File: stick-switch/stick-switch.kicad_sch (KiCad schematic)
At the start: 4 parts, among them J1 Conn_01x04

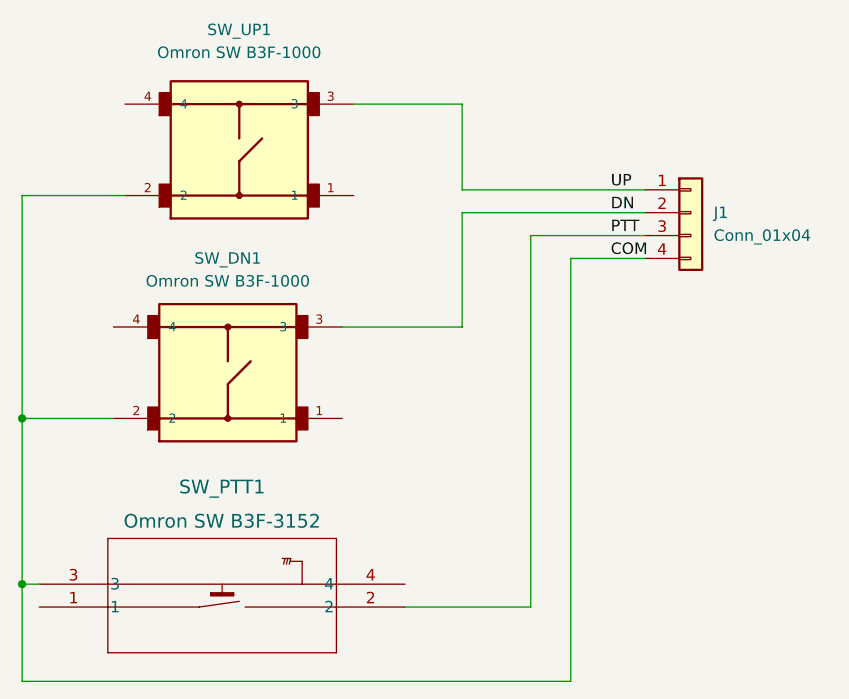
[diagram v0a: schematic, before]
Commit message: Made PTT and Trim common separate nets. Finalized layout and generated Gerbers.
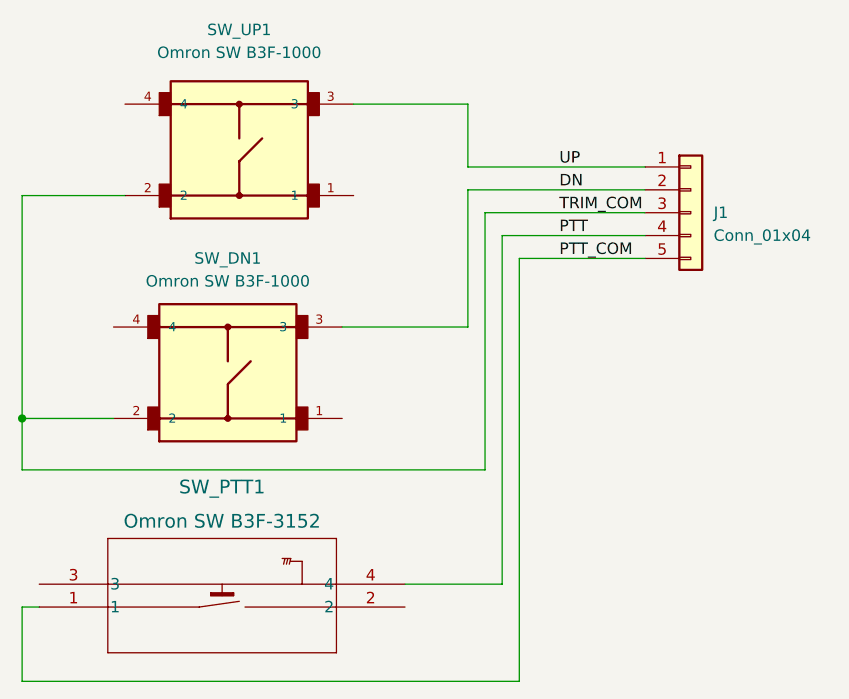
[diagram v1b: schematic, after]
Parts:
- J1: footprint Connector_PinHeader_1.27mm:PinHeader_1x04_P1.27mm_Vertical -> Connector_PinHeader_1.27mm:PinHeader_1x05_P1.27mm_Vertical; symbol Connector_Generic:Conn_01x04 -> Connector_Generic:Conn_01x05
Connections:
- net PTT: now also J1.4 (Pin_4), SW_PTT1.4; no longer J1.3 (Pin_3), SW_PTT1.2
- net PTT_COM: now reaches SW_PTT1.1
- net PTT_COM: now also J1.5 (Pin_5)
- net COM renamed TRIM_COM
- net TRIM_COM: now also J1.3 (Pin_3); no longer J1.4 (Pin_4), SW_PTT1.3
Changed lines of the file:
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@@
   (junction (at 66.675 95.25) (diameter 0) (color 0 0 0 0)
   )
-  (junction (at 66.675 113.665) (diameter 0) (color 0 0 0 0)
-  )
-  (wire (pts (xy 115.57 72.39) (xy 135.89 72.39))
+  (wire (pts (xy 116.205 69.85) (xy 135.89 69.85))
     (stroke (width 0) (type default) (color 0 0 0 0))
   )
-  (wire (pts (xy 127.635 77.47) (xy 127.635 124.46))
+  (wire (pts (xy 121.92 77.47) (xy 121.92 124.46))
     (stroke (width 0) (type default) (color 0 0 0 0))
   )
-  (wire (pts (xy 109.22 116.205) (xy 123.19 116.205))
+  (wire (pts (xy 109.22 113.665) (xy 120.015 113.665))
     (stroke (width 0) (type default) (color 0 0 0 0))
   )
@@
     (stroke (width 0) (type default) (color 0 0 0 0))
   )
-  (wire (pts (xy 115.57 60.325) (xy 115.57 69.85))
+  (wire (pts (xy 116.205 60.325) (xy 116.205 67.31))
+    (stroke (width 0) (type default) (color 0 0 0 0))
+  )
+  (wire (pts (xy 135.89 72.39) (xy 118.11 72.39))
     (stroke (width 0) (type default) (color 0 0 0 0))
   )
@@
     (stroke (width 0) (type default) (color 0 0 0 0))
   )
-  (wire (pts (xy 66.675 95.25) (xy 66.675 113.665))
+  (wire (pts (xy 103.505 60.325) (xy 116.205 60.325))
     (stroke (width 0) (type default) (color 0 0 0 0))
   )
-  (wire (pts (xy 103.505 60.325) (xy 115.57 60.325))
+  (wire (pts (xy 66.675 95.25) (xy 66.675 100.965))
     (stroke (width 0) (type default) (color 0 0 0 0))
   )
-  (wire (pts (xy 123.19 74.93) (xy 135.89 74.93))
+  (wire (pts (xy 120.015 74.93) (xy 135.89 74.93))
     (stroke (width 0) (type default) (color 0 0 0 0))
   )
-  (wire (pts (xy 115.57 69.85) (xy 135.89 69.85))
+  (wire (pts (xy 116.205 67.31) (xy 135.89 67.31))
     (stroke (width 0) (type default) (color 0 0 0 0))
   )
-  (wire (pts (xy 66.675 124.46) (xy 66.675 113.665))
+  (wire (pts (xy 66.675 124.46) (xy 66.675 116.205))
     (stroke (width 0) (type default) (color 0 0 0 0))
   )
-  (wire (pts (xy 135.89 77.47) (xy 127.635 77.47))
+  (wire (pts (xy 135.89 77.47) (xy 121.92 77.47))
     (stroke (width 0) (type default) (color 0 0 0 0))
   )
-  (wire (pts (xy 102.235 85.09) (xy 115.57 85.09))
+  (wire (pts (xy 102.235 85.09) (xy 116.205 85.09))
     (stroke (width 0) (type default) (color 0 0 0 0))
   )
-  (wire (pts (xy 66.675 113.665) (xy 68.58 113.665))
+  (wire (pts (xy 66.675 116.205) (xy 68.58 116.205))
     (stroke (width 0) (type default) (color 0 0 0 0))
   )
-  (wire (pts (xy 127.635 124.46) (xy 66.675 124.46))
+  (wire (pts (xy 118.11 100.965) (xy 66.675 100.965))
     (stroke (width 0) (type default) (color 0 0 0 0))
   )
-  (wire (pts (xy 115.57 85.09) (xy 115.57 72.39))
+  (wire (pts (xy 121.92 124.46) (xy 66.675 124.46))
     (stroke (width 0) (type default) (color 0 0 0 0))
   )
-  (wire (pts (xy 123.19 116.205) (xy 123.19 74.93))
+  (wire (pts (xy 118.11 72.39) (xy 118.11 100.965))
     (stroke (width 0) (type default) (color 0 0 0 0))
   )
-  (label "DN" (at 132.08 72.39 0)
+  (wire (pts (xy 116.205 85.09) (xy 116.205 69.85))
+    (stroke (width 0) (type default) (color 0 0 0 0))
+  )
+  (wire (pts (xy 120.015 113.665) (xy 120.015 74.93))
+    (stroke (width 0) (type default) (color 0 0 0 0))
+  )
+  (label "DN" (at 126.365 69.85 0)
     (effects (font (size 1.27 1.27)) (justify left bottom))
   )
-  (label "PTT" (at 132.08 74.93 0)
+  (label "PTT" (at 126.365 74.93 0)
     (effects (font (size 1.27 1.27)) (justify left bottom))
   )
-  (label "UP" (at 132.08 69.85 0)
+  (label "TRIM_COM" (at 126.365 72.39 0)
     (effects (font (size 1.27 1.27)) (justify left bottom))
   )
-  (label "COM" (at 132.08 77.47 0)
+  (label "UP" (at 126.365 67.31 0)
+    (effects (font (size 1.27 1.27)) (justify left bottom))
+  )
+  (label "PTT_COM" (at 126.365 77.47 0)
     (effects (font (size 1.27 1.27)) (justify left bottom))
   )
@@
     (pin "4")
   )
-  (symbol (lib_id "Connector_Generic:Conn_01x04") (at 140.97 72.39 0) (unit 1)
+  (symbol (lib_id "Connector_Generic:Conn_01x05") (at 140.97 72.39 0) (unit 1)
     (in_bom yes) (on_board yes) (fields_autoplaced)
     (property "Reference" "J1" (id 0) (at 143.51 72.3899 0)
@@
       (effects (font (size 1.27 1.27)) (justify left))
     )
-    (property "Footprint" "Connector_PinHeader_1.27mm:PinHeader_1x04_P1.27mm_Vertical" (id 2) (at 140.97 72.39 0)
+    (property "Footprint" "Connector_PinHeader_1.27mm:PinHeader_1x05_P1.27mm_Vertical" (id 2) (at 140.97 72.39 0)
       (effects (font (size 1.27 1.27)) hide)
     )
@@
     (pin "3")
     (pin "4")
+    (pin "5")
   )
   (sheet_instances
@@
   (symbol_instances
     (path "/e6c47370-49ce-4460-bd3d-460aa9989c79"
-      (reference "J1") (unit 1) (value "Conn_01x04") (footprint "Connector_PinHeader_1.27mm:PinHeader_1x04_P1.27mm_Vertical")
+      (reference "J1") (unit 1) (value "Conn_01x04") (footprint "Connector_PinHeader_1.27mm:PinHeader_1x05_P1.27mm_Vertical")
     )
     (path "/693855f7-f970-453d-b841-13f13265e856"
